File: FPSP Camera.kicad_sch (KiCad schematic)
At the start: 0 parts

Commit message: Cleanup
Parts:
- added C101, C103, C104, C105, C106, C107, C108, C109, C110, C111, C112, C113, C114, C115, C119, C122: 100n, Capacitor_SMD:C_0603_1608Metric_Pad1.08x0.95mm_HandSolder, symbol Device:C
- added C102, C116, C117, C118: 4.7u, Capacitor_SMD:C_0603_1608Metric_Pad1.08x0.95mm_HandSolder, symbol Device:C
- added C120: 0.1u, Capacitor_SMD:C_0603_1608Metric_Pad1.08x0.95mm_HandSolder, symbol Device:C
- added C121: 22pF, Capacitor_SMD:C_0603_1608Metric_Pad1.08x0.95mm_HandSolder, symbol Device:C
- added C123, C124, C125, C126, C127, C128: 1u, Capacitor_SMD:C_0603_1608Metric_Pad1.08x0.95mm_HandSolder, symbol Device:C
- added D101, D102, D103, D104: LED, Diode_SMD:D_0603_1608Metric, symbol Device:LED
- added H101, H102, H103, H104: MountingHole, MountingHole:MountingHole_2.7mm_M2.5, symbol Mechanical:MountingHole
- added J101: Conn_01x24_Socket, Connector_FFC-FPC:TE_2-84952-4_1x24-1MP_P1.0mm_Horizontal, symbol Connector:Conn_01x24_Socket
- added J102: SM03B-SRSS-TB, Connector_JST:JST_SH_SM03B-SRSS-TB_1x03-1MP_P1.00mm_Horizontal, symbol Connector_Generic_MountingPin:Conn_01x03_MountingPin
- added J103: USB_B_Micro, RP2350_60QFN_minimal:USB_Micro-B_Amphenol_10103594-0001LF_Horizontal_modified, symbol Connector:USB_B_Micro
- added J104: Conn_02x06_Odd_Even, Connector_PinHeader_2.54mm:PinHeader_2x06_P2.54mm_Vertical, symbol Connector_Generic:Conn_02x06_Odd_Even
- added JP101, JP102: SolderJumper_2_Open, Jumper:SolderJumper-2_P1.3mm_Open_RoundedPad1.0x1.5mm, symbol Jumper:SolderJumper_2_Open
- added L101: 3.3u, Inductor_SMD:L_1210_3225Metric, symbol Device:L
- added R101, R102, R103, R111, R112, R113, R117, R121, R122, R123, R124: 10k, Resistor_SMD:R_0603_1608Metric_Pad0.98x0.95mm_HandSolder, symbol Device:R
- added R104: 33, Resistor_SMD:R_0603_1608Metric_Pad0.98x0.95mm_HandSolder, symbol Device:R
- added R105, R106: 27, Resistor_SMD:R_0603_1608Metric_Pad0.98x0.95mm_HandSolder, symbol Device:R
- added R107, R110, R114: DNF, Resistor_SMD:R_0603_1608Metric_Pad0.98x0.95mm_HandSolder, symbol Device:R
- added R108, R119: 1k, Resistor_SMD:R_0603_1608Metric_Pad0.98x0.95mm_HandSolder, symbol Device:R
- added R109: 0, Resistor_SMD:R_0603_1608Metric_Pad0.98x0.95mm_HandSolder, symbol Device:R
- added R115, R116, R118, R120: 0R, Resistor_SMD:R_0603_1608Metric_Pad0.98x0.95mm_HandSolder, symbol Device:R
- added TP101: TestPoint, TestPoint:TestPoint_Pad_D1.0mm, symbol Connector:TestPoint
- added U101: ASM330LHHXTR, ASM330LHHXTR:XDCR_ASM330LHHXTR, symbol ASM330LHHXTR:ASM330LHHXTR
- added U102: W25Q128JVS, Package_SO:SOIC-8_5.3x5.3mm_P1.27mm, symbol Memory_Flash:W25Q128JVS
- added U103: RP2350_60QFN, projLib:RP2350-QFN-60-1EP_7x7_P0.4mm_EP3.4x3.4mm_ThermalVias, symbol MCU_RaspberryPi_RP2350:RP2350_60QFN
- added U104: TLV75533PDRV, Package_SON:WSON-6-1EP_2x2mm_P0.65mm_EP1x1.6mm, symbol Regulator_Linear:TLV75533PDRV
- added U105: TLV73328PDRV, Package_SON:WSON-6-1EP_2x2mm_P0.65mm_EP1x1.6mm, symbol Regulator_Linear:TLV75533PDRV
- added U106: TLV73315PDRV, Package_SON:WSON-6-1EP_2x2mm_P0.65mm_EP1x1.6mm, symbol Regulator_Linear:TLV75533PDRV
- added Y101: SiT8008xx-1x-xxE, Oscillator:Oscillator_SMD_SiT_PQFN-4Pin_2.5x2.0mm, symbol Oscillator:SiT8008xx-1x-xxE
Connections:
- new net: R105.2, U103.52 (USB_DP)
- new net: R106.2, U103.51 (USB_DM)
- new net: JP102.2 (B), R119.2
- new net: R114.1, U103.21 (XIN)
- new net: D103.2 (A), R123.2
- new net: D102.2 (A), R122.2
- new net: D104.2 (A), R124.2
- new net: D101.2 (A), R121.2
- new net: U101.10 (NC), U101.11 (NC), U101.6 (NC)
- new net +1V1: C101.1, C102.1, C103.1, C118.1, L101.1, TP101.1, U103.23 (DVDD), U103.39 (DVDD), U103.50 (VREG_FB), U103.6 (DVDD)
- new net +1V5: C128.1, J101.10 (Pin_10), R124.1, U106.1 (OUT)
- new net +2V8: C126.1, J101.4 (Pin_4), R123.1, U105.1 (OUT)
- new net +3.3V: C104.1, C105.1, C106.1, C107.1, C108.1, C109.1, C110.1, C111.1, C112.1, C113.1, C114.1, C115.1, C117.1, C119.1, C122.1, C124.1, C125.1, C127.1, J101.11 (Pin_11), R101.1, R102.1, R103.1, R104.1, R107.1, R111.1, R112.1, R113.1, R115.2, R122.1, U101.2 (MSDA), U101.3 (MSCL), U101.5 (VDD_IO), U101.8 (VDD), U102.8 (VCC), U103.1 (IOVDD), U103.11 (IOVDD), U103.20 (IOVDD), U103.30 (IOVDD), U103.38 (IOVDD), U103.44 (ADC_AVDD), U103.45 (IOVDD), U103.49 (VREG_VIN), U103.53 (USB_OTP_VDD), U103.54 (QSPI_IOVDD), U104.1 (OUT), U105.4 (EN), U105.6 (IN), U106.4 (EN), U106.6 (IN), Y101.1 (OE), Y101.4 (Vdd)
- new net +5V: C123.1, R121.1, U104.4 (EN), U104.6 (IN)
- new net CS_1: U101.12 (CS), U103.3 (GPIO1)
- new net DATA0_1: J101.24 (Pin_24)
- new net DATA1_1: J101.23 (Pin_23), R115.1
- new net DATA2_1: J101.19 (Pin_19), U103.19 (GPIO15)
- new net DATA3_1: J101.21 (Pin_21), U103.28 (GPIO17)
- new net DATA4_1: J101.22 (Pin_22), U103.29 (GPIO18)
- new net DATA5_1: J101.20 (Pin_20), U103.27 (GPIO16)
- new net DATA6_1: J101.18 (Pin_18), U103.18 (GPIO14)
- new net DATA7_1: J101.16 (Pin_16), U103.16 (GPIO12)
- new net DATA8_1: J101.14 (Pin_14), U103.15 (GPIO11)
- new net DATA9_1: J101.12 (Pin_12), U103.31 (GPIO19)
- new net DGND: J101.15 (Pin_15), R120.2
- new net EXT_XCLK_1: R116.2, U103.32 (GPIO20)
- new net FLASH_SS_1: R107.2, R109.1, R110.1, U102.1 (~{CS})
- new net GND: C101.2, C102.2, C103.2, C104.2, C105.2, C106.2, C107.2, C108.2, C109.2, C110.2, C111.2, C112.2, C113.2, C114.2, C115.2, C116.2, C117.2, C118.2, C119.2, C120.2, C121.2, C122.2, C123.2, C124.2, C125.2, C126.2, C127.2, C128.2, D101.1 (K), D102.1 (K), D103.1 (K), D104.1 (K), J101.2 (Pin_2), J102.2 (Pin_2), J102.MP (MountPin), J103.5 (GND), J103.6 (Shield), J104.10 (Pin_10), J104.12 (Pin_12), J104.8 (Pin_8), JP101.1 (A), JP102.1 (A), R117.2, R120.1, U101.7 (GND), U102.4 (GND), U103.47 (VREG_PGND), U103.61 (GND), U104.3 (GND), U104.7 (GND), U105.3 (GND), U105.7 (GND), U106.3 (GND), U106.7 (GND), Y101.2 (GND)
- new net GPIO0_1: R110.2, U103.2 (GPIO0)
- new net HSYNC_1: J101.9 (Pin_9), U103.33 (GPIO21)
- new net IMAGE_OUT_1_1: J104.2 (Pin_2), U103.35 (GPIO23)
- new net IMAGE_OUT_2_1: J104.4 (Pin_4), U103.36 (GPIO24)
- new net INT1_1: U101.4 (INT1), U103.8 (GPIO5)
- new net INT2_1: U101.9 (INT2), U103.9 (GPIO6)
- new net INT_XCLK: R118.2, U103.34 (GPIO22)
- new net PCLK_1: C121.1, J101.17 (Pin_17), U103.17 (GPIO13)
- new net POSITION_OUT_1: J104.6 (Pin_6), U103.37 (GPIO25)
- new net PWDN_1: J101.8 (Pin_8), R117.1
- new net QSPI_SCLK_1: U102.6 (CLK), U103.56 (QSPI_SCLK)
- new net QSPI_SD0_1: U102.5 (DI/IO_{0}), U103.57 (QSPI_SD0)
- new net QSPI_SD1_1: U102.2 (DO/IO_{1}), U103.59 (QSPI_SD1)
- new net QSPI_SD2_1: U102.3 (~{WP}/IO_{2}), U103.58 (QSPI_SD2)
- new net QSPI_SD3_1: U102.7 (~{HOLD}/~{RESET}/IO_{3}), U103.55 (QSPI_SD3)
- new net QSPI_SS_1: R108.1, R109.2, U103.60 (QSPI_SS)
- new net RUN_1: R119.1, U103.26 (RUN)
- new net SCL_cam_1: J101.5 (Pin_5), R112.2, U103.13 (GPIO9)
- new net SCL_imu_1: R103.2, U101.13 (SCL), U103.7 (GPIO4)
- new net SDA_cam_1: J101.3 (Pin_3), R111.2, U103.12 (GPIO8)
- new net SDA_imu_1: R102.2, U101.14 (SDA), U103.5 (GPIO3)
- new net SDO_imu_1: R101.2, U101.1 (SDO/SA0), U103.4 (GPIO2)
- new net SWCLK_1: J102.1 (Pin_1), U103.24 (SWCLK)
- new net SWD_1: J102.3 (Pin_3), U103.25 (SWD)
- new net USB_D1+: J103.3 (D+), R105.1
- new net USB_D1-: J103.2 (D-), R106.1
- new net VREG_AVDD_1: C116.1, R104.2, U103.46 (VREG_AVDD)
- new net VREG_LX_1: L101.2, U103.48 (VREG_LX)
- new net VSYNC_1: J101.7 (Pin_7), U103.10 (GPIO7)
- new net XCLK: J101.13 (Pin_13), R116.1, R118.1
- new net XIN_mem1: R114.2, Y101.3 (OUT)
- new net ~{RESET_1}: C120.1, J101.6 (Pin_6), R113.2, U103.14 (GPIO10)
- new net ~{USB_BOOT_1}: JP101.2 (B), R108.2
- no-connect marks 0 -> 15
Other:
- removed sheet IMU
- removed sheet IOs
- removed sheet MCU
- removed sheet Power
- note added: "! CHANGE CONNECTOR TYPE"
- note added: "0Ω if works well"
- note added: "1.5 V"
- note added: "12 MHz OSC"
- note added: "2.8 V"
- note added: "3.3 V"
- note added: "I2C configuration: CS = Vdd"
- note added: "IMU1"
- note added: "JST Debug Connector"
- note added: "LED indicator"
- note added: "MCU"
- note added: "MCU1"
- note added: "OUT to FPGA"
- note added: "OV5640 I/O"

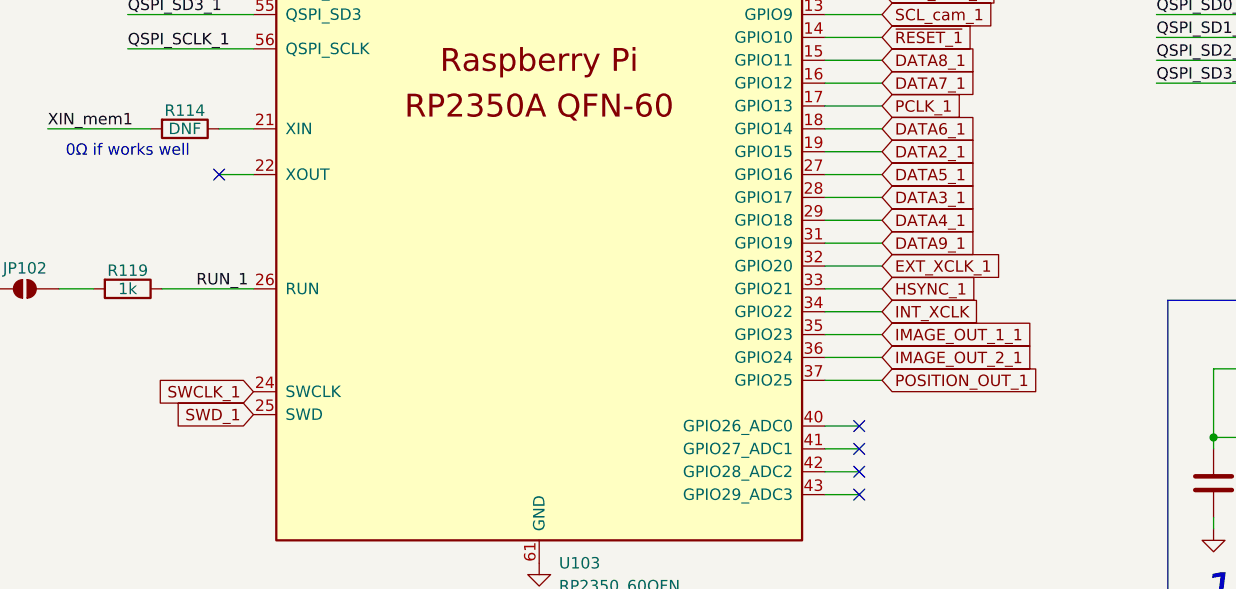
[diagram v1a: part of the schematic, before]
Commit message: Reassigned MCU Pinout
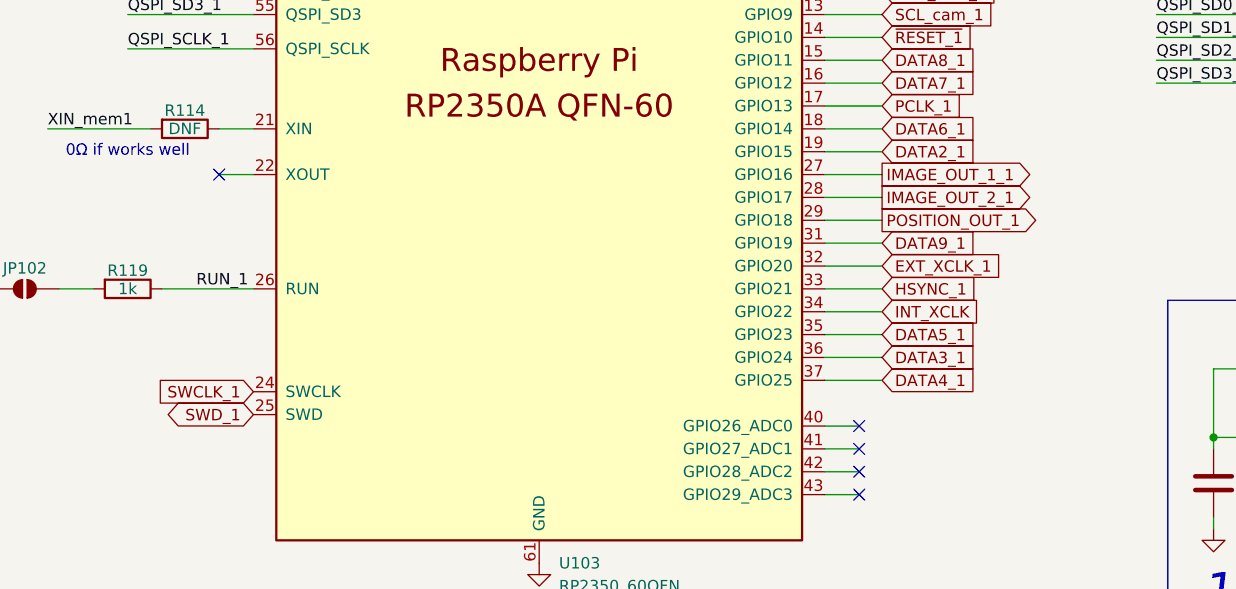
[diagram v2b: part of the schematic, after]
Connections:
- net DATA3_1: now also U103.36 (GPIO24); no longer U103.28 (GPIO17)
- net DATA4_1: now also U103.37 (GPIO25); no longer U103.29 (GPIO18)
- net DATA5_1: now also U103.35 (GPIO23); no longer U103.27 (GPIO16)
- net IMAGE_OUT_1_1: now also U103.27 (GPIO16); no longer U103.35 (GPIO23)
- net IMAGE_OUT_2_1: now also U103.28 (GPIO17); no longer U103.36 (GPIO24)
- net POSITION_OUT_1: now also U103.29 (GPIO18); no longer U103.37 (GPIO25)

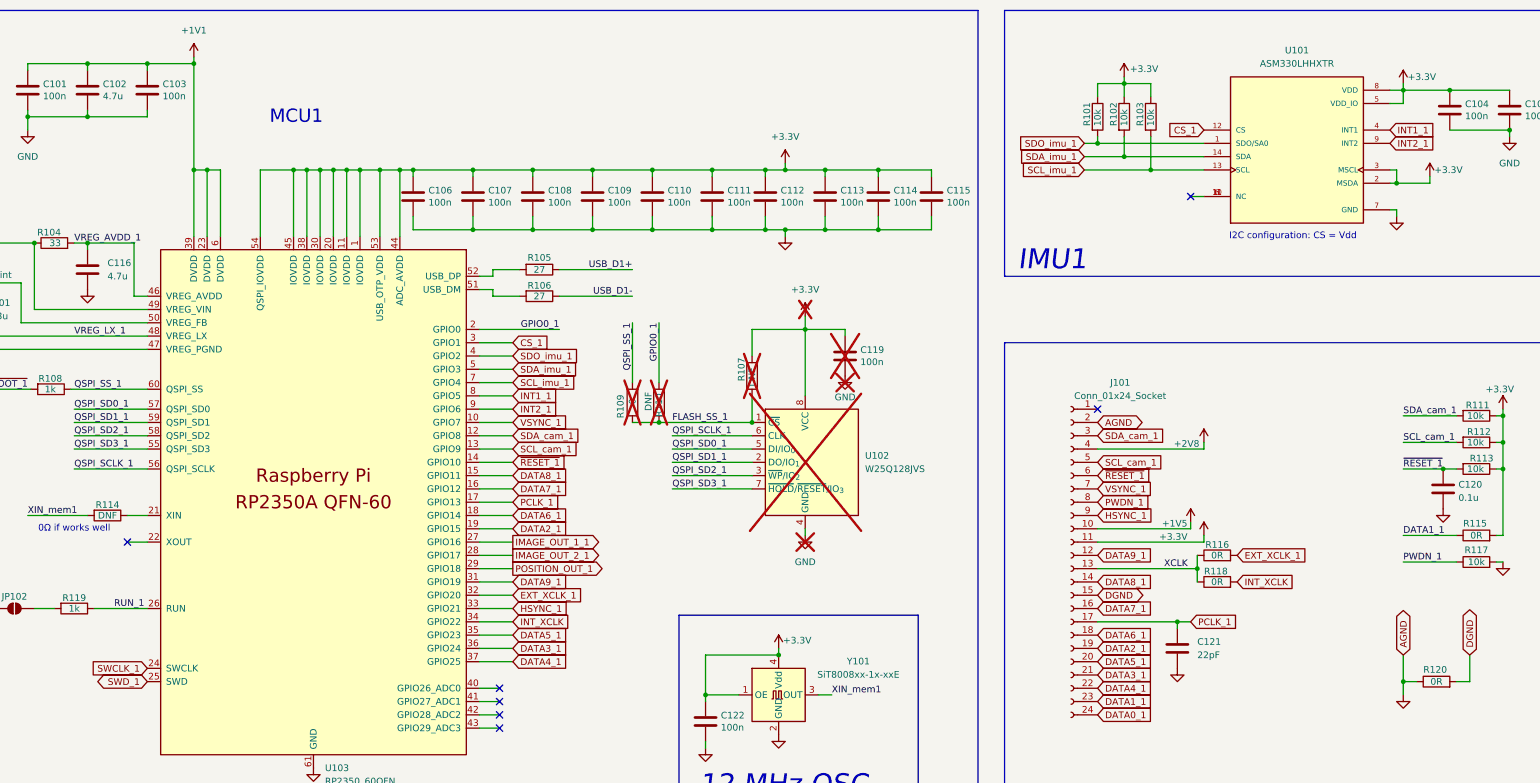
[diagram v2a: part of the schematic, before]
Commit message: IMU Changed to ICM-45686
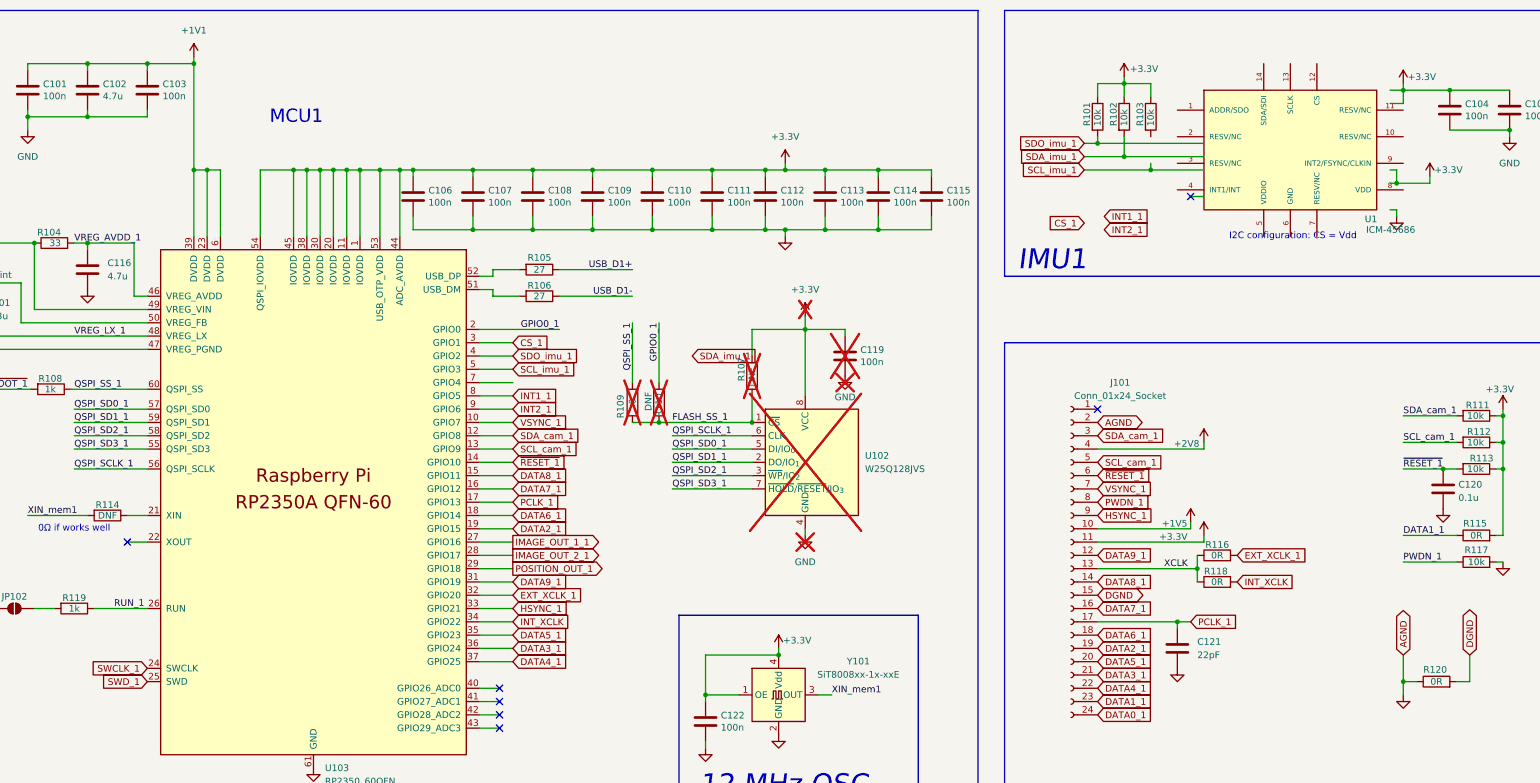
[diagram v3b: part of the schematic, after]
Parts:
- removed U101: ASM330LHHXTR, ASM330LHHXTR:XDCR_ASM330LHHXTR, symbol ASM330LHHXTR:ASM330LHHXTR
- added U1: ICM-45686, ICM-45686:IC_ICM-45686, symbol ICM-45686:ICM-45686
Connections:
- net SCL_imu_1: now also U103.5 (GPIO3); no longer R103.2, U103.7 (GPIO4)
- net SDA_imu_1: no longer U103.5 (GPIO3)

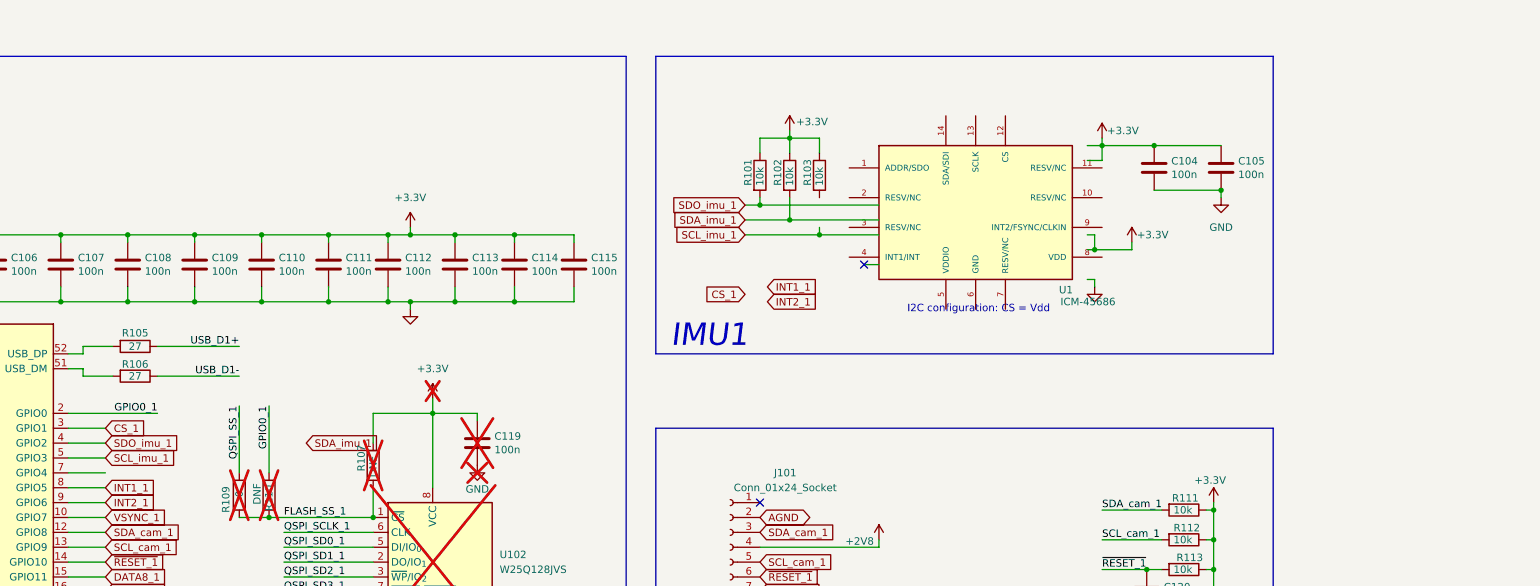
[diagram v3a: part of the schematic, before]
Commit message: IMU Subsystem Change
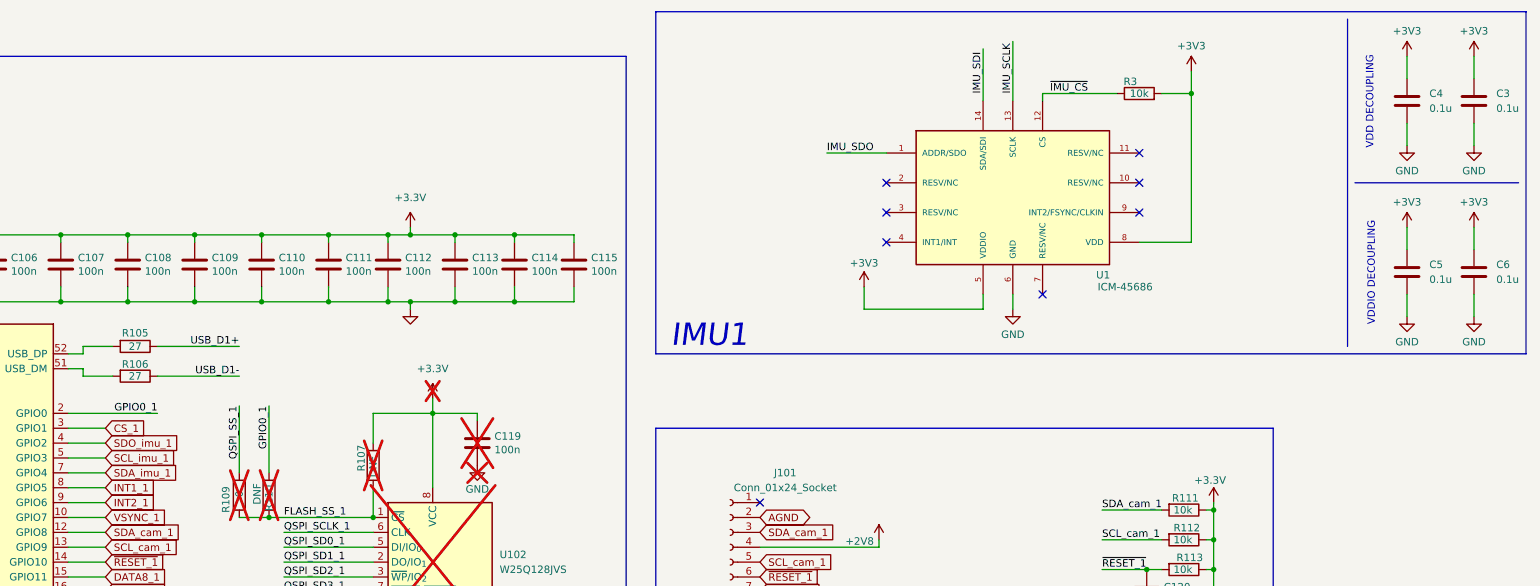
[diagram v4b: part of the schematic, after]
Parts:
- removed C104, C105: 100n, Capacitor_SMD:C_0603_1608Metric_Pad1.08x0.95mm_HandSolder, symbol Device:C
- removed R101, R102, R103: 10k, Resistor_SMD:R_0603_1608Metric_Pad0.98x0.95mm_HandSolder, symbol Device:R
- added C3, C4, C5, C6: 0.1u, Capacitor_SMD:C_0402_1005Metric_Pad0.74x0.62mm_HandSolder, symbol Device:C
- added R3: 10k, Resistor_SMD:R_0402_1005Metric_Pad0.72x0.64mm_HandSolder, symbol Device:R
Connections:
- net GND: now also U1.6 (GND), C3.2, C4.2, C5.2, C6.2
- net SDA_imu_1: now also U103.7 (GPIO4)
- net IMU_SDO: now reaches U1.1 (ADDR/SDO)
- net ~{IMU_CS}: now reaches U1.12 (CS)
- net ~{IMU_CS}: now also R3.1
- net IMU_SCLK: now reaches U1.13 (SCLK)
- net IMU_SDI: now reaches U1.14 (SDA/SDI)
- net +3V3: now reaches U1.5 (VDDIO)
- net +3V3: now also U1.8 (VDD), C3.1, C4.1, C5.1, C6.1, R3.2
- no-connect marks 15 -> 21
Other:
- note added: "VDD DECOUPLING"
- note added: "VDDIO DECOUPLING"
- note removed: "I2C configuration: CS = Vdd"
- moved on the sheet: U1
